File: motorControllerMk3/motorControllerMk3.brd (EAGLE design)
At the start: 54.6 x 49.2 mm, 43 parts, among them J1 AVR_SPI_PRG_6NS, Y1 16MHz

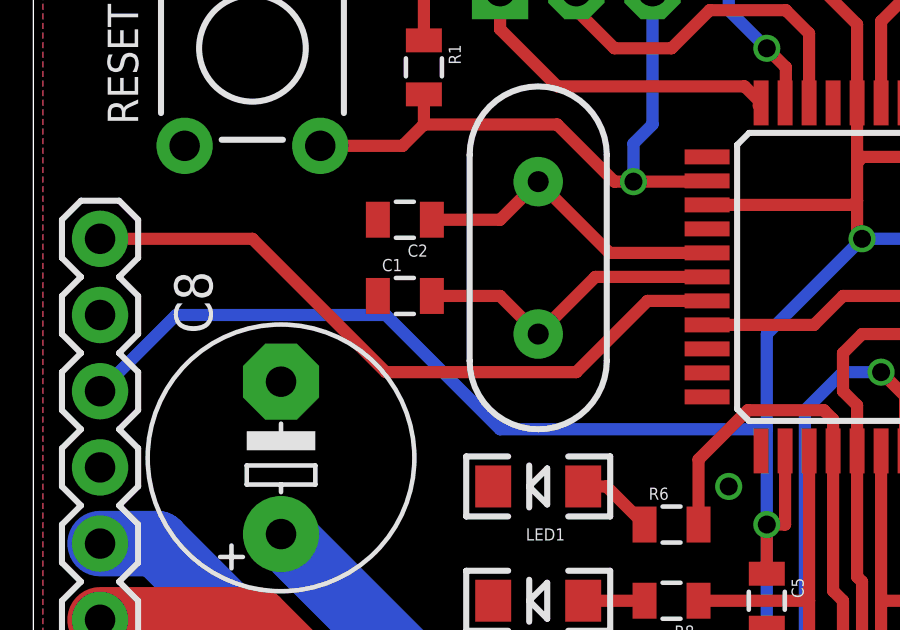
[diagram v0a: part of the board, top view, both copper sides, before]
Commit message: more space on crystal
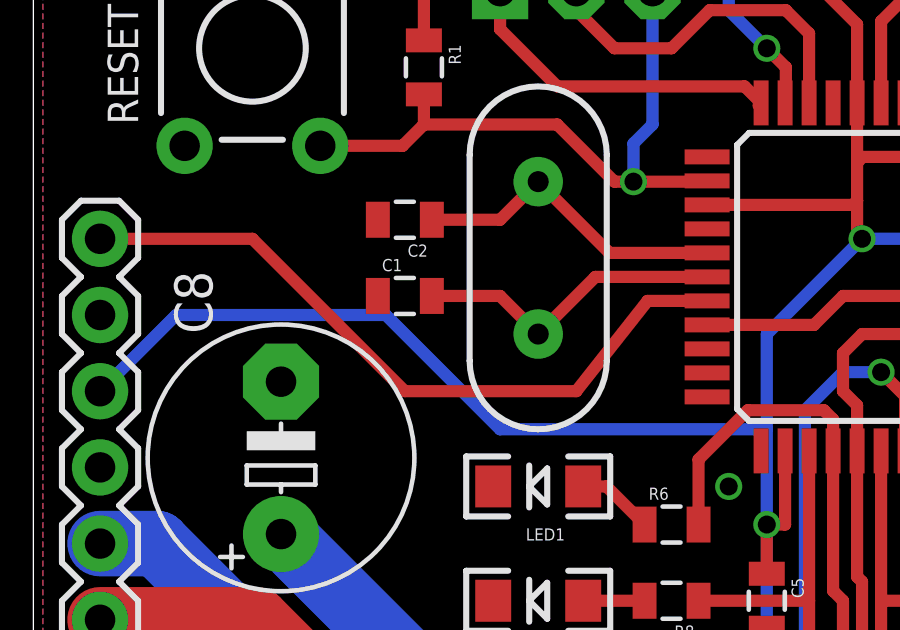
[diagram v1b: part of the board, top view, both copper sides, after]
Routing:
- net PD0: track 23.1 -> 23.8 mm
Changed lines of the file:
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@@
 </signal>
 <signal name="PD0">
-<wire x1="34.925" y1="40.64" x2="41.275" y2="40.64" width="0.4064" layer="1"/>
-<wire x1="41.275" y1="40.64" x2="43.65" y2="43.015" width="0.4064" layer="1"/>
+<wire x1="35.56" y1="40.005" x2="41.275" y2="40.005" width="0.4064" layer="1"/>
+<wire x1="41.275" y1="40.005" x2="43.65" y2="43.015" width="0.4064" layer="1"/>
 <contactref element="JP2" pad="6"/>
 <wire x1="30.48" y1="45.085" x2="25.4" y2="45.085" width="0.4064" layer="1"/>
 <contactref element="U$2" pad="18"/>
 <wire x1="43.65" y1="43.015" x2="45.635" y2="43.015" width="0.4064" layer="1"/>
-<wire x1="30.48" y1="45.085" x2="34.925" y2="40.64" width="0.4064" layer="1"/>
+<wire x1="30.48" y1="45.085" x2="35.56" y2="40.005" width="0.4064" layer="1"/>
 </signal>
 <signal name="PD1">

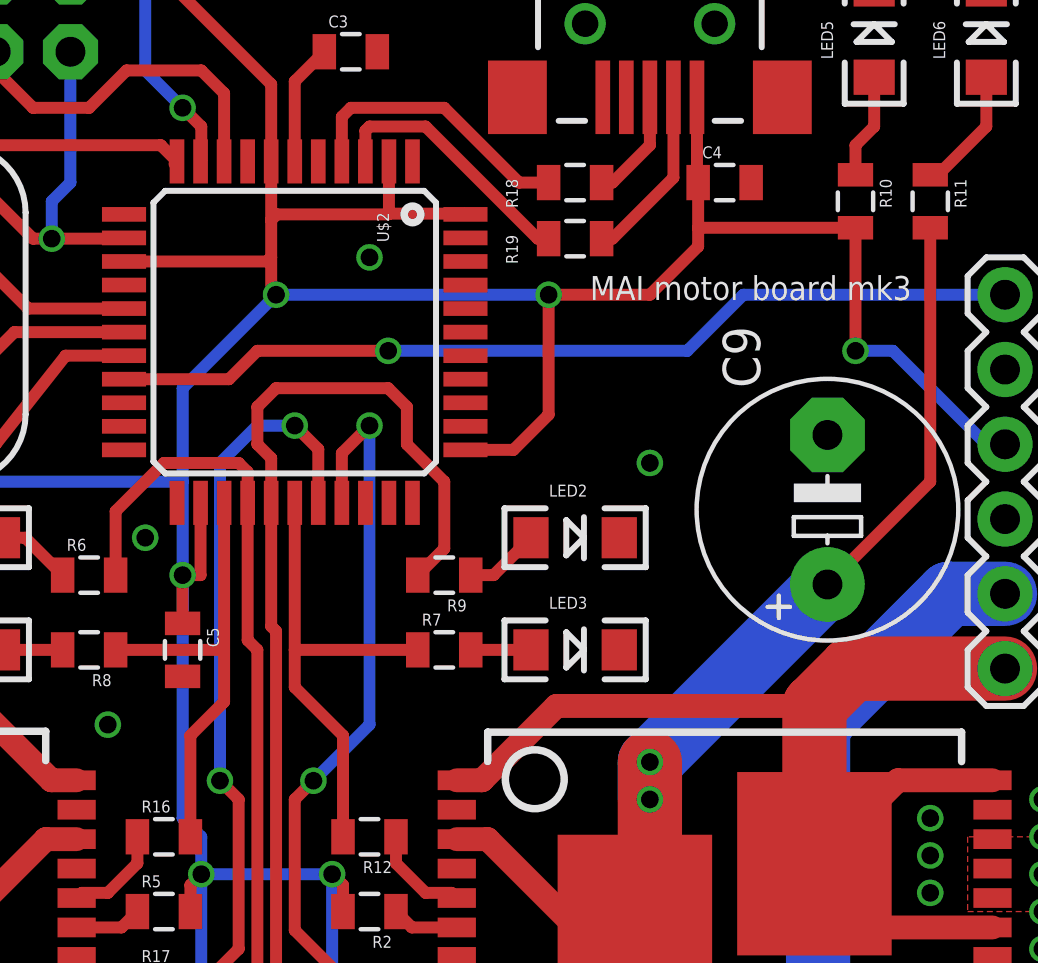
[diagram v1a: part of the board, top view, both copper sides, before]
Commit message: changed some traces to be shorter
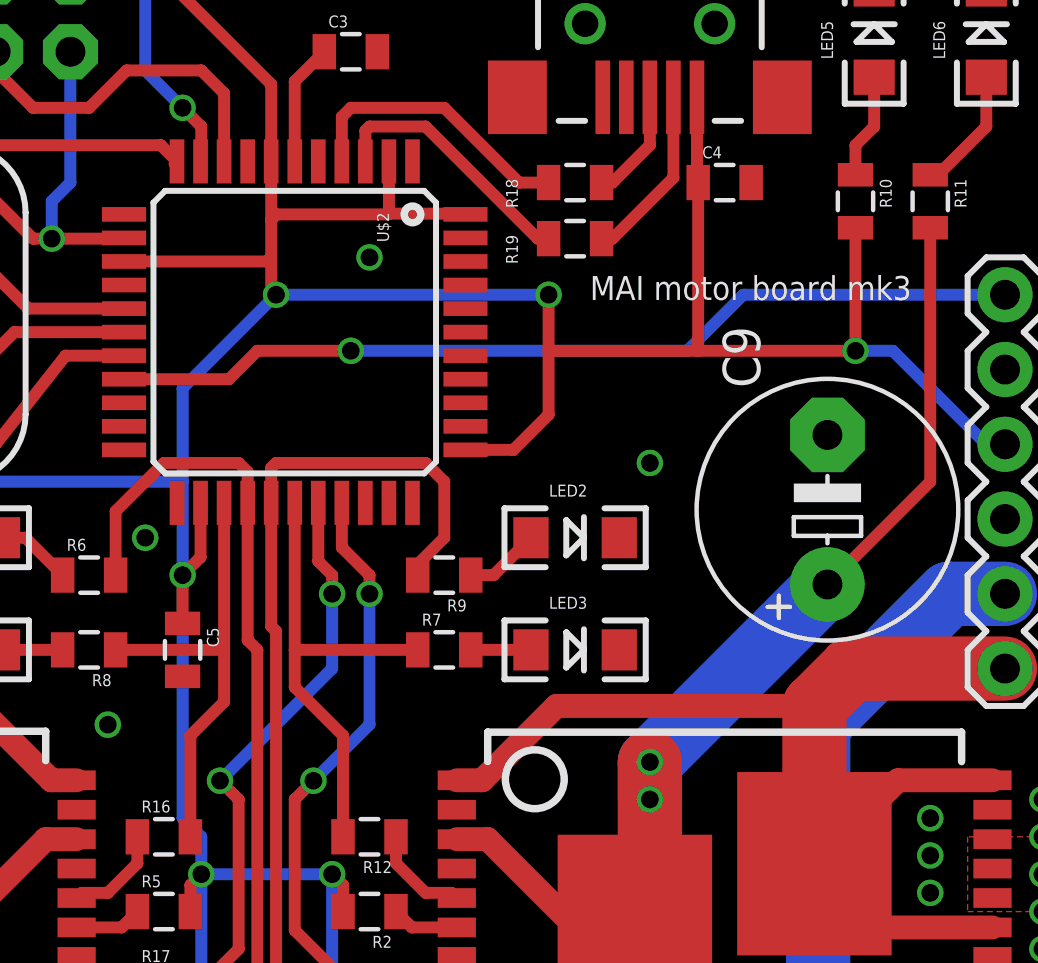
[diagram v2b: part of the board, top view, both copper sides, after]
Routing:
- net PB5: track 25.0 -> 19.4 mm
- net PB6: track 24.2 -> 18.9 mm
- net PD7: track 38.6 -> 33.8 mm
- net +5V: track 156.6 -> 159.1 mm
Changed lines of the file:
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@@
 <?xml version="1.0" encoding="utf-8"?>
 <!DOCTYPE eagle SYSTEM "eagle.dtd">
-<eagle version="6.5.0">
+<eagle version="6.3">
 <drawing>
 <settings>
@@
 <wire x1="48.26" y1="26.67" x2="47.625" y2="27.305" width="0.4064" layer="16"/>
 <wire x1="47.625" y1="27.305" x2="47.625" y2="35.56" width="0.4064" layer="16"/>
-<wire x1="70.485" y1="47.36" x2="70.485" y2="43.18" width="0.4064" layer="1"/>
-<wire x1="48.235" y1="38.015" x2="48.235" y2="35.56" width="0.4064" layer="1"/>
-<wire x1="48.235" y1="35.56" x2="47.625" y2="35.56" width="0.4064" layer="1"/>
 <wire x1="65.1" y1="51.7925" x2="65.1" y2="48.895" width="0.4064" layer="1"/>
 <wire x1="65.1" y1="48.895" x2="65.14" y2="48.895" width="0.4064" layer="1"/>
@@
 <wire x1="34.925" y1="42.545" x2="38.735" y2="38.735" width="0.4064" layer="16"/>
 <wire x1="38.735" y1="38.735" x2="47.625" y2="38.735" width="0.4064" layer="16"/>
-<wire x1="60.06" y1="45.085" x2="63.5" y2="45.085" width="0.4064" layer="1"/>
-<wire x1="63.5" y1="45.085" x2="65.14" y2="46.725" width="0.4064" layer="1"/>
-<wire x1="65.14" y1="48.895" x2="65.14" y2="47.36" width="0.4064" layer="1"/>
-<wire x1="65.14" y1="47.36" x2="65.14" y2="46.725" width="0.4064" layer="1"/>
-<wire x1="70.485" y1="47.36" x2="65.14" y2="47.36" width="0.4064" layer="1"/>
 <via x="60.06" y="45.085" extent="1-16" drill="0.6" shape="square"/>
 <wire x1="47.625" y1="33.92" x2="47.625" y2="35.56" width="0.4064" layer="1"/>
 <wire x1="57.235" y1="39.815" x2="58.865" y2="39.815" width="0.4064" layer="1"/>
 <wire x1="58.865" y1="39.815" x2="60.06" y2="41.01" width="0.4064" layer="1"/>
-<wire x1="60.06" y1="41.01" x2="60.06" y2="45.085" width="0.4064" layer="1"/>
+<wire x1="60.06" y1="41.01" x2="60.06" y2="43.18" width="0.4064" layer="1"/>
+<wire x1="60.06" y1="43.18" x2="60.06" y2="45.085" width="0.4064" layer="1"/>
 <wire x1="60.06" y1="45.085" x2="50.8" y2="45.085" width="0.4064" layer="16"/>
+<wire x1="48.235" y1="38.015" x2="48.235" y2="36.17" width="0.4064" layer="1"/>
+<wire x1="48.235" y1="36.17" x2="47.625" y2="35.56" width="0.4064" layer="1"/>
+<wire x1="70.485" y1="43.18" x2="65.14" y2="43.18" width="0.4064" layer="1"/>
+<wire x1="65.14" y1="43.18" x2="60.06" y2="43.18" width="0.4064" layer="1"/>
+<wire x1="65.14" y1="48.895" x2="65.14" y2="43.18" width="0.4064" layer="1"/>
+<wire x1="70.485" y1="47.36" x2="70.485" y2="43.18" width="0.4064" layer="1"/>
 </signal>
 <signal name="GND">
@@
 <wire x1="49.53" y1="27.94" x2="48.895" y2="28.575" width="0.4064" layer="1"/>
 <via x="48.895" y="28.575" extent="1-16" drill="0.6" shape="square"/>
-<wire x1="48.895" y1="28.575" x2="48.895" y2="39.37" width="0.4064" layer="16"/>
-<via x="51.435" y="40.64" extent="1-16" drill="0.6" shape="square"/>
-<wire x1="51.435" y1="40.64" x2="52.235" y2="39.84" width="0.4064" layer="1"/>
-<wire x1="48.895" y1="39.37" x2="50.165" y2="40.64" width="0.4064" layer="16"/>
-<wire x1="50.165" y1="40.64" x2="51.435" y2="40.64" width="0.4064" layer="16"/>
+<via x="52.705" y="34.925" extent="1-16" drill="0.6" shape="square"/>
 <contactref element="U$2" pad="29"/>
-<wire x1="52.235" y1="38.015" x2="52.235" y2="39.84" width="0.4064" layer="1"/>
+<wire x1="52.705" y1="34.925" x2="52.705" y2="32.385" width="0.4064" layer="16"/>
+<wire x1="52.705" y1="32.385" x2="48.895" y2="28.575" width="0.4064" layer="16"/>
+<wire x1="52.235" y1="38.015" x2="52.235" y2="36.03" width="0.4064" layer="1"/>
+<wire x1="52.235" y1="36.03" x2="52.705" y2="35.56" width="0.4064" layer="1"/>
+<wire x1="52.705" y1="35.56" x2="52.705" y2="34.925" width="0.4064" layer="1"/>
 </signal>
 <signal name="PB6">
@@
 <wire x1="53.34" y1="21.59" x2="51.435" y2="23.495" width="0.4064" layer="1"/>
 <wire x1="51.435" y1="23.495" x2="51.435" y2="27.94" width="0.4064" layer="1"/>
-<wire x1="53.035" y1="39.7" x2="53.975" y2="40.64" width="0.4064" layer="1"/>
-<via x="53.975" y="40.64" extent="1-16" drill="0.6" shape="square"/>
-<wire x1="53.975" y1="40.64" x2="53.975" y2="30.48" width="0.4064" layer="16"/>
-<wire x1="53.975" y1="30.48" x2="52.07" y2="28.575" width="0.4064" layer="16"/>
+<via x="53.975" y="34.925" extent="1-16" drill="0.6" shape="square"/>
 <via x="52.07" y="28.575" extent="1-16" drill="0.6" shape="square"/>
 <wire x1="52.07" y1="28.575" x2="51.435" y2="27.94" width="0.4064" layer="1"/>
 <contactref element="U$2" pad="30"/>
-<wire x1="53.035" y1="38.015" x2="53.035" y2="39.7" width="0.4064" layer="1"/>
+<wire x1="53.975" y1="34.925" x2="53.975" y2="30.48" width="0.4064" layer="16"/>
+<wire x1="53.975" y1="30.48" x2="52.07" y2="28.575" width="0.4064" layer="16"/>
+<wire x1="53.035" y1="38.015" x2="53.035" y2="36.5" width="0.4064" layer="1"/>
+<wire x1="53.035" y1="36.5" x2="53.975" y2="35.56" width="0.4064" layer="1"/>
+<wire x1="53.975" y1="35.56" x2="53.975" y2="34.925" width="0.4064" layer="1"/>
 </signal>
 <signal name="N$10">
@@
 <signal name="PD1">
 <wire x1="49.2" y1="42.215" x2="50.165" y2="43.18" width="0.4064" layer="1"/>
-<wire x1="50.165" y1="43.18" x2="54.61" y2="43.18" width="0.4064" layer="1"/>
-<via x="54.61" y="43.18" extent="1-16" drill="0.6" shape="square"/>
+<wire x1="50.165" y1="43.18" x2="53.34" y2="43.18" width="0.4064" layer="1"/>
+<via x="53.34" y="43.18" extent="1-16" drill="0.6" shape="square"/>
 <contactref element="JP1" pad="6"/>
 <contactref element="U$2" pad="19"/>
 <wire x1="49.2" y1="42.215" x2="45.635" y2="42.215" width="0.4064" layer="1"/>
-<wire x1="54.61" y1="43.18" x2="64.77" y2="43.18" width="0.4064" layer="16"/>
+<wire x1="53.34" y1="43.18" x2="64.77" y2="43.18" width="0.4064" layer="16"/>
 <wire x1="64.77" y1="43.18" x2="66.675" y2="45.085" width="0.4064" layer="16"/>
 <wire x1="66.675" y1="45.085" x2="75.565" y2="45.085" width="0.4064" layer="16"/>
@@
 <wire x1="50.8" y1="19.05" x2="50.8" y2="33.655" width="0.4064" layer="1"/>
 <wire x1="50.635" y1="33.82" x2="50.8" y2="33.655" width="0.4064" layer="1"/>
-<wire x1="55.245" y1="40.005" x2="55.245" y2="41.275" width="0.4064" layer="1"/>
-<wire x1="55.245" y1="41.275" x2="54.61" y2="41.91" width="0.4064" layer="1"/>
-<wire x1="54.61" y1="41.91" x2="50.8" y2="41.91" width="0.4064" layer="1"/>
-<wire x1="50.635" y1="39.535" x2="50.165" y2="40.005" width="0.4064" layer="1"/>
-<wire x1="50.165" y1="40.005" x2="50.165" y2="41.275" width="0.4064" layer="1"/>
-<wire x1="50.165" y1="41.275" x2="50.8" y2="41.91" width="0.4064" layer="1"/>
 <contactref element="U$2" pad="27"/>
 <wire x1="50.635" y1="38.015" x2="50.635" y2="33.82" width="0.4064" layer="1"/>
-<wire x1="50.635" y1="38.015" x2="50.635" y2="39.535" width="0.4064" layer="1"/>
-<wire x1="55.245" y1="40.005" x2="56.515" y2="38.735" width="0.4064" layer="1"/>
-<wire x1="56.515" y1="38.735" x2="56.515" y2="36.46" width="0.4064" layer="1"/>
-<wire x1="56.515" y1="36.46" x2="55.615" y2="35.56" width="0.4064" layer="1"/>
+<wire x1="55.615" y1="35.56" x2="55.615" y2="35.93" width="0.4064" layer="1"/>
+<wire x1="55.615" y1="35.93" x2="56.515" y2="36.83" width="0.4064" layer="1"/>
+<wire x1="56.515" y1="36.83" x2="56.515" y2="38.735" width="0.4064" layer="1"/>
+<wire x1="56.515" y1="38.735" x2="55.88" y2="39.37" width="0.4064" layer="1"/>
+<wire x1="55.88" y1="39.37" x2="50.8" y2="39.37" width="0.4064" layer="1"/>
+<wire x1="50.635" y1="38.015" x2="50.635" y2="39.205" width="0.4064" layer="1"/>
+<wire x1="50.635" y1="39.205" x2="50.8" y2="39.37" width="0.4064" layer="1"/>
 </signal>
 <signal name="N$22">
@@
 </signal>
 </signals>
-<errors>
-</errors>
 </board>
 </drawing>
